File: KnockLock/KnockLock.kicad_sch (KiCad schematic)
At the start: 30 parts, among them IC1 ESP32-C3-WROOM-02-N4, IC2 LM2575-3.3WT, IC3 MC74HC74ADTR2G, J1 2477, J2 UJ20-C-H-G-TH-P16-TR, U1 ADXL345BCCZ-RL7

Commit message: Minor Adjustments + Footprints
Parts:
- R3, R4, R5, R7: footprint (none) -> SamacSys_Parts:RESAD1590W60L630D240
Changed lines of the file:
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@@
 			)
 		)
-		(property "Footprint" ""
+		(property "Footprint" "SamacSys_Parts:RESAD1590W60L630D240"
 			(at 223.52 70.358 90)
 			(effects
@@
 			)
 		)
-		(property "Footprint" ""
+		(property "Footprint" "SamacSys_Parts:RESAD1590W60L630D240"
 			(at 107.95 90.678 90)
 			(effects
@@
 			)
 		)
-		(property "Footprint" ""
+		(property "Footprint" "SamacSys_Parts:RESAD1590W60L630D240"
 			(at 223.52 65.278 90)
 			(effects
@@
 			)
 		)
-		(property "Footprint" ""
+		(property "Footprint" "SamacSys_Parts:RESAD1590W60L630D240"
 			(at 223.52 67.818 90)
 			(effects

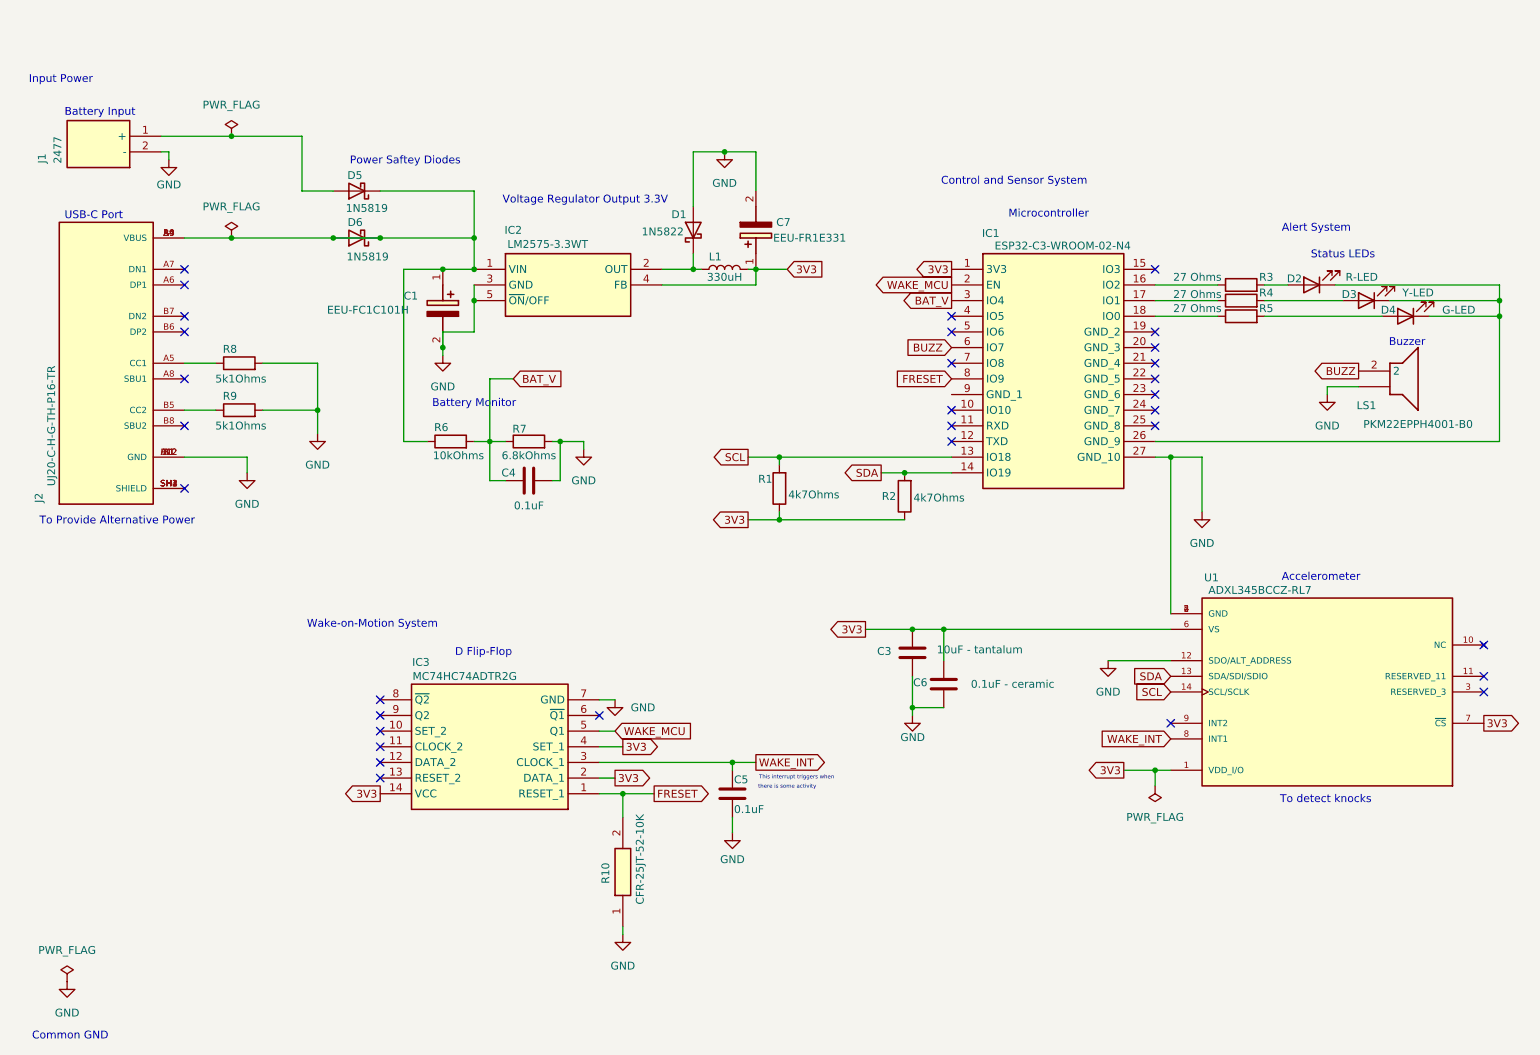
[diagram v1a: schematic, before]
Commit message: v1.3 of schematic with servo motor connection
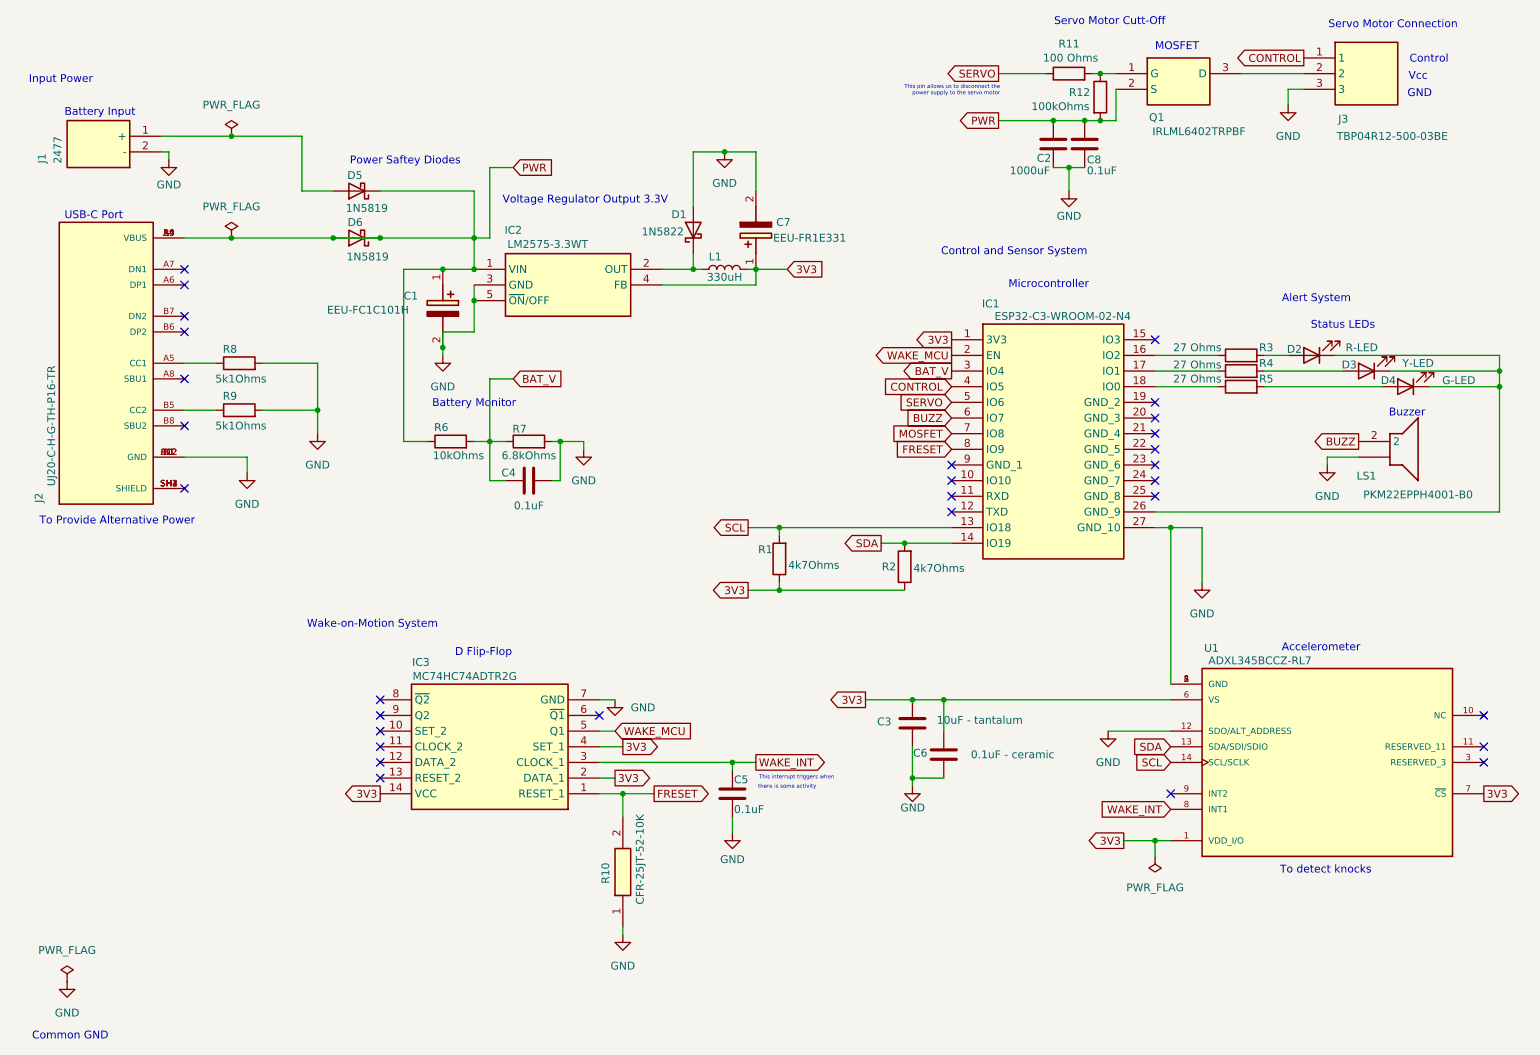
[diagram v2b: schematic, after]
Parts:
- added C2: 1000uF, symbol Device:C
- added C8: 0.1uF, symbol Device:C
- added J3: TBP04R12-500-03BE, TBP04R1250003BE, symbol SamacSys_Parts:TBP04R12-500-03BE
- added Q1: IRLML6402TRPBF, SOT95P237X112-3N, symbol SamacSys_Parts:IRLML6402TRPBF
- added R11: 100 Ohms, symbol Device:R
- added R12: 100kOhms, symbol Device:R
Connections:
- net GND: now also C2.1, C8.1, J3.3
- net PWR: now reaches C1.1 (+), D5.1 (K), D6.1 (K), D6.2 (A), IC2.1 (VIN), J2.A4 (VBUS), J2.A9 (VBUS), J2.B4 (VBUS), J2.B9 (VBUS), R6.1
- net PWR: now also C2.2, C8.2, Q1.2 (S), R12.2
- net CONTROL: now reaches IC1.4 (IO5)
- net CONTROL: now also J3.1
- net SERVO: now reaches IC1.5 (IO6)
- net SERVO: now also R11.1
- net MOSFET: now reaches IC1.7 (IO8)
- new net: J3.2, Q1.3 (D)
- new net: Q1.1 (G), R11.2, R12.1
- no-connect marks 32 -> 30
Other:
- note added: "Control"
- note added: "GND"
- note added: "MOSFET"
- note added: "Servo Motor Connection"
- note added: "Servo Motor Cutt-Off"
- note added: "This pin allows us to disconnect the power supply to the servo motor"
- note added: "Vcc"
- moved on the sheet: C3, C6, D2, D3, D4, IC1, LS1, R1, R2, R3, R4, R5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
